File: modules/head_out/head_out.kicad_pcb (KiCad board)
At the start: 2 copper layers, 30.5 x 68.6 mm, 4 parts

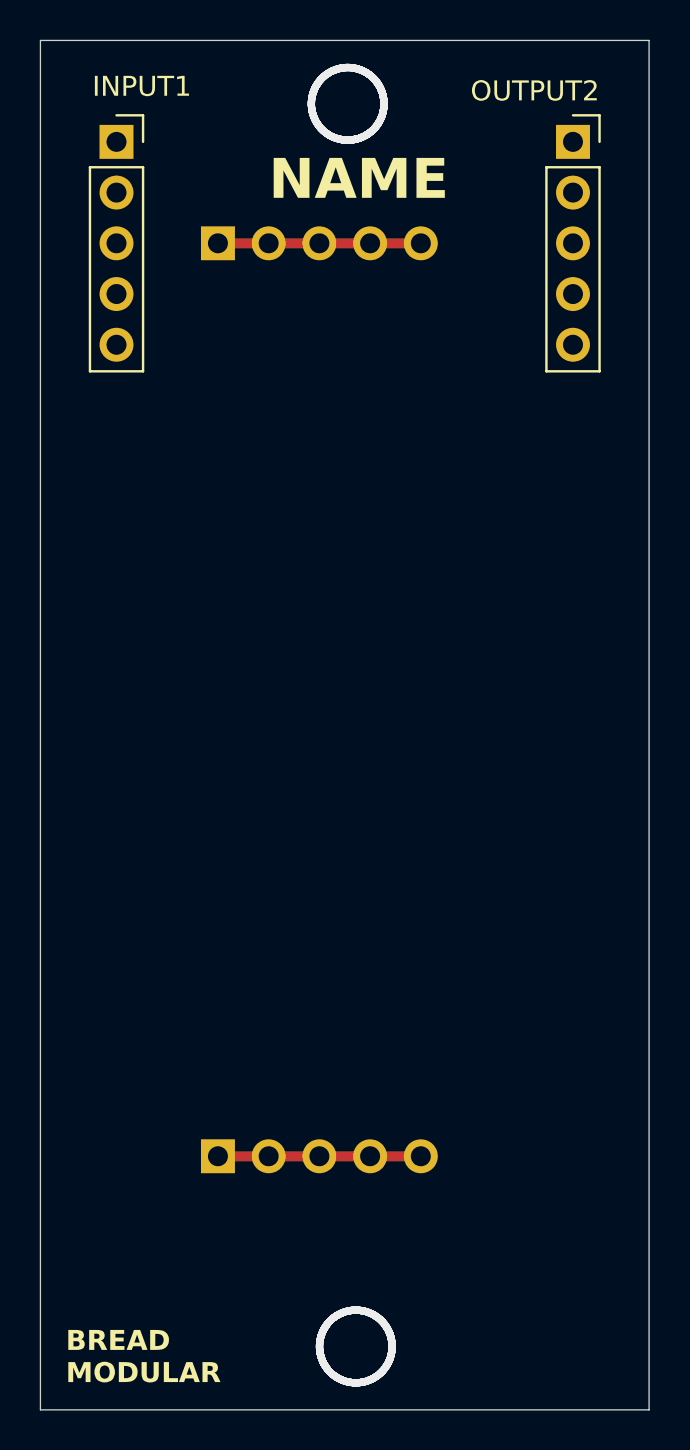
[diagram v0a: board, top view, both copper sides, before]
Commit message: Finished pcb_design of the head_out
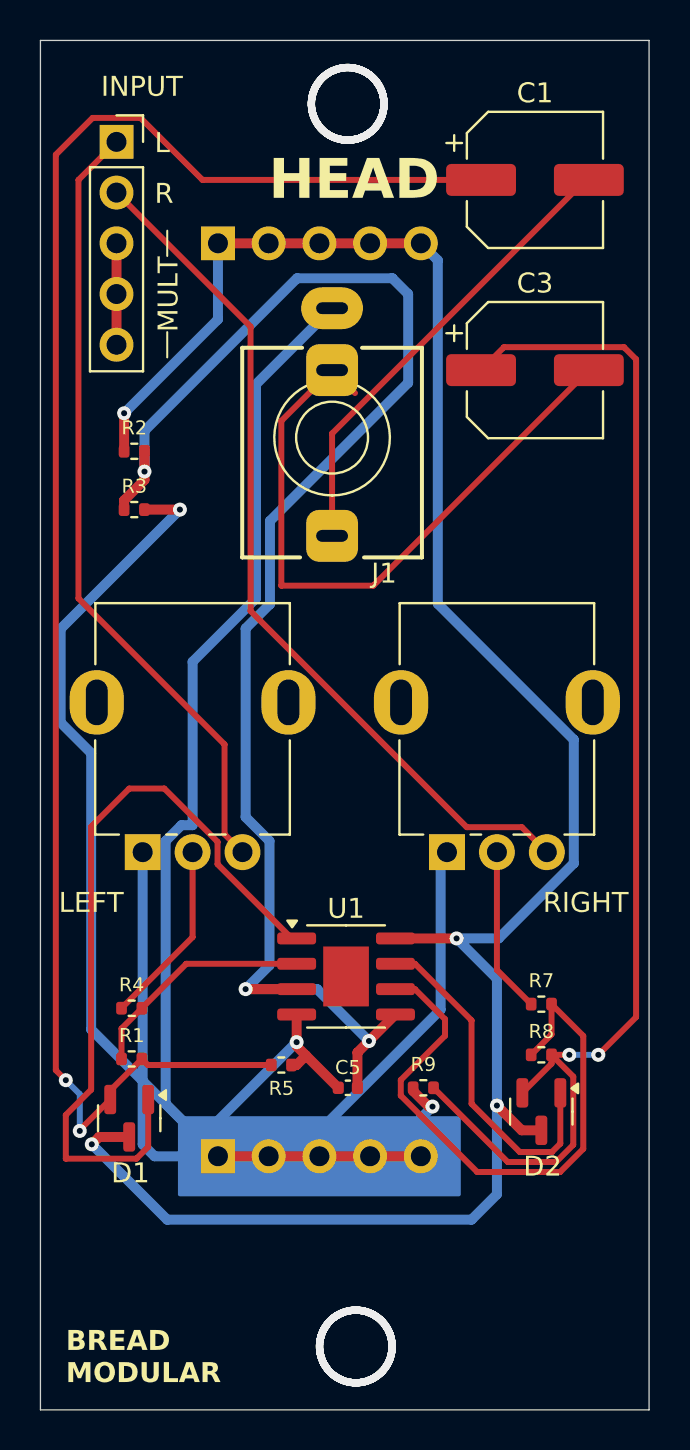
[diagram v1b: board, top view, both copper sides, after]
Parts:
- removed OUTPUT2: Conn_01x05_Socket, Connector_PinSocket_2.54mm:PinSocket_1x05_P2.54mm_Vertical
- added C1: 470uf, Capacitor_SMD:CP_Elec_6.3x7.7, F.Cu at (71.8, 47.6)
- added C3: 470uf, Capacitor_SMD:CP_Elec_6.3x7.7, F.Cu at (71.8, 57.1)
- added C5: 0.1uf, Capacitor_SMD:C_0402_1005Metric, F.Cu at (62.4, 93.1)
- added D1: SS8050, Package_TO_SOT_SMD:SOT-23, F.Cu at (51.4, 94.6)
- added D2: SS8050, Package_TO_SOT_SMD:SOT-23, F.Cu at (72.1, 94.3)
- added J1: AudioJack3, BreadModular_AudioJacks:Jack_3.5mm_QingPu_WQP-PJ366ST_Vertical, F.Cu at (61.6, 60.5)
- added LEFT: 50k, BreadModular_Pots:Potentiometer_RV09, F.Cu at (52.1, 81.3)
- added R1: 22k, Resistor_SMD:R_0402_1005Metric, F.Cu at (51.6, 91.6)
- added R2: 1k, Resistor_SMD:R_0402_1005Metric, F.Cu at (51.7, 61.2)
- added R3: 1k, Resistor_SMD:R_0402_1005Metric, F.Cu at (51.7, 64.1)
- added R4: 100k, Resistor_SMD:R_0402_1005Metric, F.Cu at (51.6, 89.1)
- added R5: 110, Resistor_SMD:R_0402_1005Metric, F.Cu at (59.1, 92.0)
- added R7: 100k, Resistor_SMD:R_0402_1005Metric, F.Cu at (72.1, 88.9)
- added R8: 22k, Resistor_SMD:R_0402_1005Metric, F.Cu at (72.1, 91.4)
- added R9: 110, Resistor_SMD:R_0402_1005Metric, F.Cu at (66.2, 93.1)
- added RIGHT: 50k, BreadModular_Pots:Potentiometer_RV09, F.Cu at (67.3, 81.3)
- added U1: MCP6002-xSN, Package_SO:SOIC-8-1EP_3.9x4.9mm_P1.27mm_EP2.29x3mm, F.Cu at (62.3, 87.5)
- renumbered INPUT1 to INPUT
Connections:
- net Net-(5V1-Pin_1) renamed +5V
- INPUT pad 1: unconnected-(INPUT1-Pin_1-Pad1) -> IN_L
- INPUT pad 2: unconnected-(INPUT1-Pin_2-Pad2) -> IN_R
- INPUT pad 3: unconnected-(INPUT1-Pin_3-Pad3) -> Net-(INPUT1-Pin_3)
- INPUT pad 4: unconnected-(INPUT1-Pin_4-Pad4) -> Net-(INPUT1-Pin_3)
- INPUT pad 5: unconnected-(INPUT1-Pin_5-Pad5) -> Net-(INPUT1-Pin_3)
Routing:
- net GND: track 10.2 -> 164.3 mm, vias 0 -> 3
- net +5V: track 10.2 -> 108.0 mm, vias 0 -> 4
- net Net-(C1-Pad1): track 0.00 -> 84.2 mm, vias 0 -> 2
- net +2.5V: track 0.00 -> 75.5 mm, vias 0 -> 3
- net Net-(C3-Pad1): track 0.00 -> 62.8 mm, vias 0 -> 2
- net IN_R: track 0.00 -> 43.6 mm
- net IN_L: track 0.00 -> 39.8 mm
- net Net-(D1-K-Pad1): track 0.00 -> 38.7 mm
- net OUT_R: track 0.00 -> 33.3 mm
- net Net-(U1B--): track 0.00 -> 29.9 mm
- net OUT_L: track 0.00 -> 23.2 mm
- net Net-(D2-K-Pad1): track 0.00 -> 17.3 mm
- net Net-(U1A--): track 0.00 -> 11.6 mm
- net Net-(R4-Pad1): track 0.00 -> 9.29 mm
- net Net-(R7-Pad1): track 0.00 -> 8.32 mm
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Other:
- board text added: "HEAD"
- board text added: "L"
- board text added: "MULT"
- board text added: "R"
- board text removed: "NAME"

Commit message: Finialize the design based on actual wattage requirements.
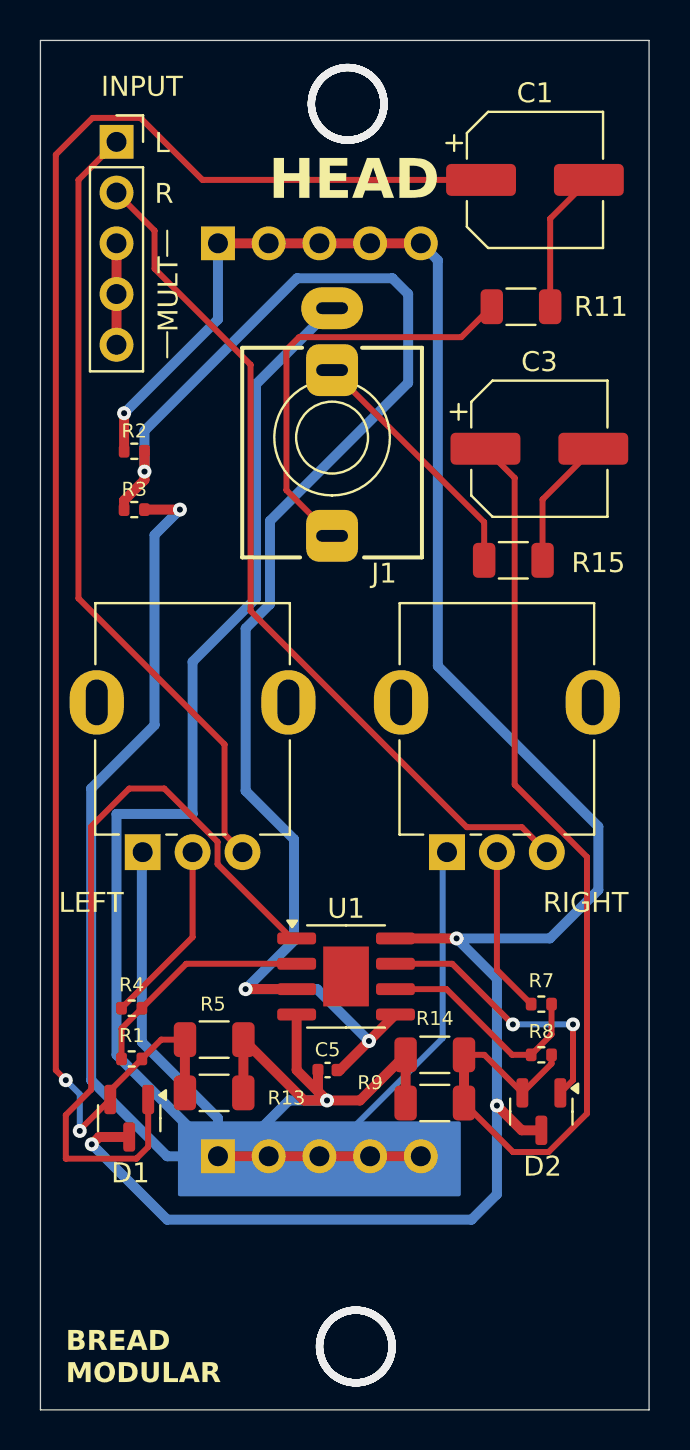
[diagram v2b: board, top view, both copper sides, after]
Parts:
- added R11: 10, Resistor_SMD:R_1206_3216Metric, F.Cu at (71.1, 54.0)
- added R13: 220, Resistor_SMD:R_1206_3216Metric, F.Cu at (55.7, 93.3)
- added R14: 220, Resistor_SMD:R_1206_3216Metric, F.Cu at (66.7, 91.4)
- added R15: 10, Resistor_SMD:R_1206_3216Metric, F.Cu at (70.7, 66.7)
- R5, R9: value 110 -> 220; footprint Resistor_SMD:R_0402_1005Metric -> Resistor_SMD:R_1206_3216Metric
- moved C3 3.94 mm to (72.0, 61.1)
- moved R5 3.60 mm to (55.7, 90.7)
- moved C5 1.35 mm to (61.4, 92.2)
- moved R9 0.95 mm to (66.7, 93.9)
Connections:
- C1 pad 2: OUT_L -> Net-(C1-Pad2)
- C3 pad 2: OUT_R -> Net-(C3-Pad2)
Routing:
- net OUT_R: track 33.3 -> 12.7 mm
- net Net-(U1B--): track 29.9 -> 11.1 mm
- net Net-(C3-Pad1): track 62.8 -> 52.0 mm, vias 2 -> 0
- net Net-(C1-Pad2): track 0.00 -> 7.15 mm
- net Net-(C3-Pad2): track 0.00 -> 6.64 mm
- net Net-(D2-K-Pad1): track 17.3 -> 13.9 mm, vias 0 -> 2
- net +5V: track 108.0 -> 110.5 mm
- net OUT_L: track 23.2 -> 21.4 mm
- net Net-(C1-Pad1): track 84.2 -> 82.9 mm
- net GND: track 164.3 -> 165.2 mm, vias 3 -> 2
- net +2.5V: track 75.5 -> 76.2 mm

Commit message: Finalize the head_out module.
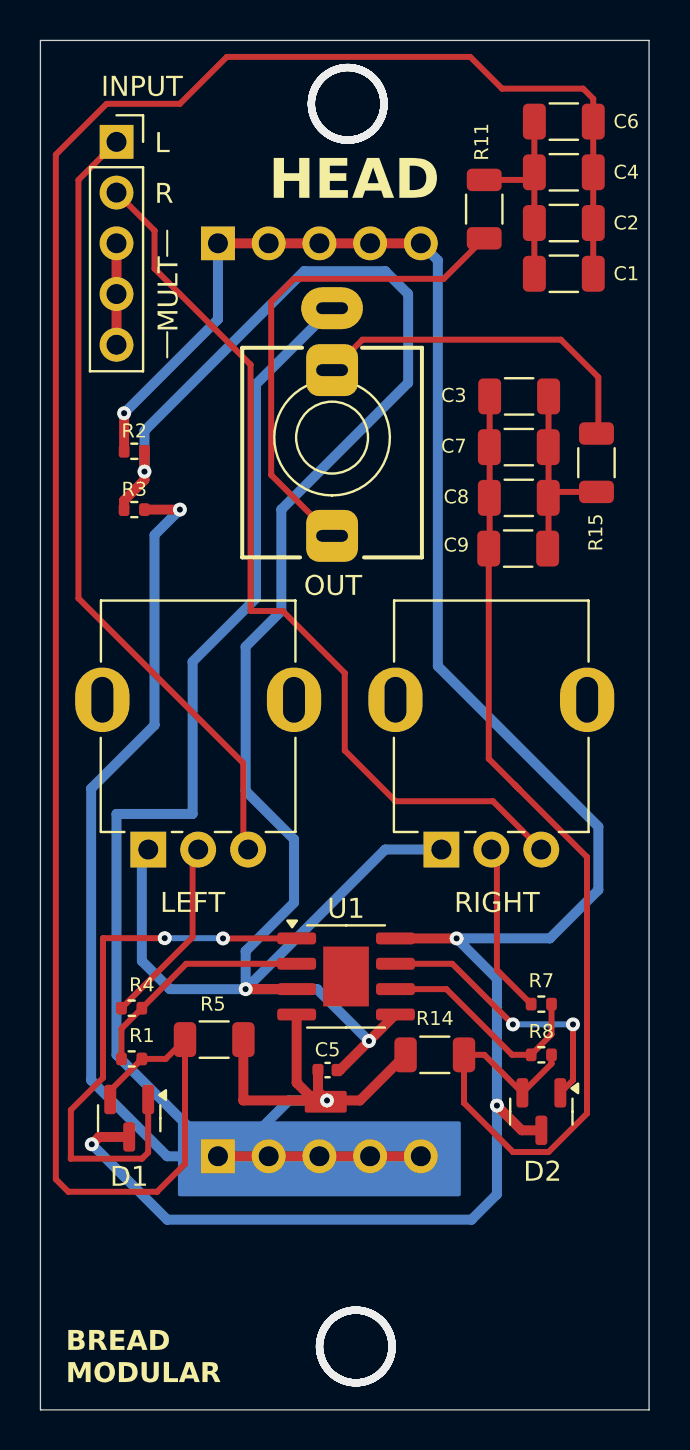
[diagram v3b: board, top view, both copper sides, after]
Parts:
- removed R13, R9: 220, Resistor_SMD:R_1206_3216Metric
- added C2: 100uf, Capacitor_SMD:C_1206_3216Metric, F.Cu at (73.2, 49.8)
- added C4: 100uf, Capacitor_SMD:C_1206_3216Metric, F.Cu at (73.2, 47.2)
- added C6: 100uf, Capacitor_SMD:C_1206_3216Metric, F.Cu at (73.2, 44.7)
- added C7: 100uf, Capacitor_SMD:C_1206_3216Metric, F.Cu at (70.9, 61.0)
- added C8: 100uf, Capacitor_SMD:C_1206_3216Metric, F.Cu at (70.9, 63.5)
- added C9: 100uf, Capacitor_SMD:C_1206_3216Metric, F.Cu at (70.9, 66.1)
- C1, C3: value 470uf -> 100uf; footprint Capacitor_SMD:CP_Elec_6.3x7.7 -> Capacitor_SMD:C_1206_3216Metric
- R14, R5: value 220 -> 100
- moved R15 6.42 mm to (74.8, 61.8), turned to -90 degrees
- moved R11 5.22 mm to (69.2, 49.1), turned to 90 degrees
- moved C1 4.92 mm to (73.2, 52.3), turned to 180 degrees
- moved C3 2.81 mm to (71.0, 58.5)
- moved LEFT 0.31 mm to (52.4, 81.2)
- moved RIGHT 0.31 mm to (67.1, 81.2)
- renumbered J1 to OUT
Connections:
- LEFT pad 1: GND -> +2.5V
- RIGHT pad 1: GND -> +2.5V
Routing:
- net GND: track 165.2 -> 127.3 mm
- net Net-(C1-Pad1): track 82.9 -> 108.9 mm, vias 2 -> 0
- net +2.5V: track 76.2 -> 100.6 mm
- net Net-(D1-K-Pad1): track 38.7 -> 28.2 mm, vias 0 -> 2
- net OUT_R: track 12.7 -> 17.6 mm
- net Net-(C1-Pad2): track 7.15 -> 11.2 mm
- net Net-(C3-Pad2): track 6.64 -> 10.3 mm
- net OUT_L: track 21.4 -> 25.0 mm
- net Net-(C3-Pad1): track 52.0 -> 54.7 mm
- net IN_R: track 43.6 -> 45.5 mm
